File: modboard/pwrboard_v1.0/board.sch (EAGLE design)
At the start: 28 parts, among them J2 POWER_JACKPTH

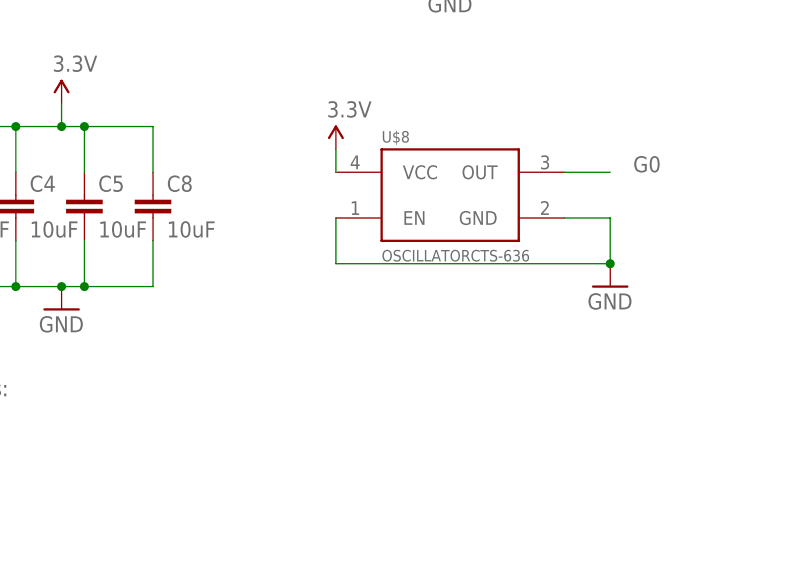
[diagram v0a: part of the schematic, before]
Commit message: re-done version of the vga board, using a spartan-6 tqfp, and following the reference design
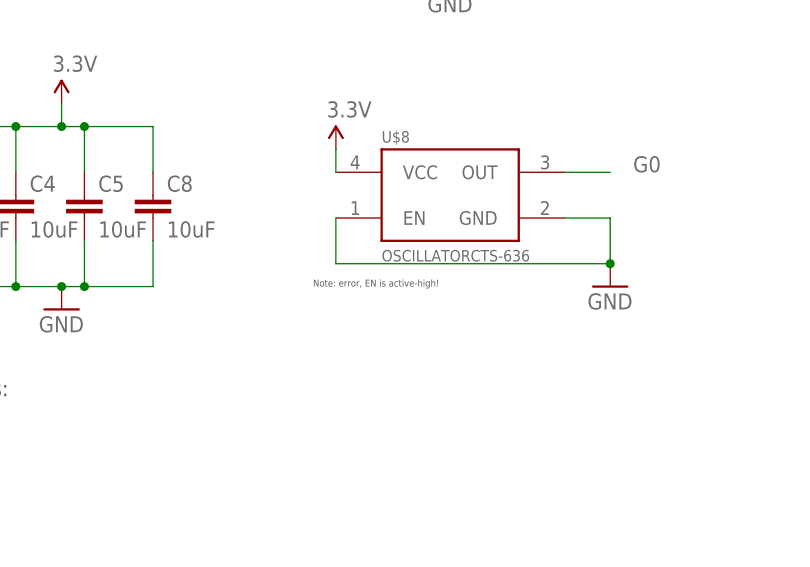
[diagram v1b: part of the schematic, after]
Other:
- note added: "Note: error, EN is active-high!"
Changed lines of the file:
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@@
 1.5nF
 12.1k</text>
+<text x="33.02" y="-111.76" size="0.762" layer="97">Note: error, EN is active-high!</text>
 </plain>
 <instances>
